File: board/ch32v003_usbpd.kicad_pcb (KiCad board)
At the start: 2 copper layers, 32 x 35 mm, 21 parts, among them J1 USB_C_Receptacle_USB2.0, J2 Conn_01x04_Pin, J3 VOUT, U1 CH32V003F4P6, U2 HT75xx-1-SOT89

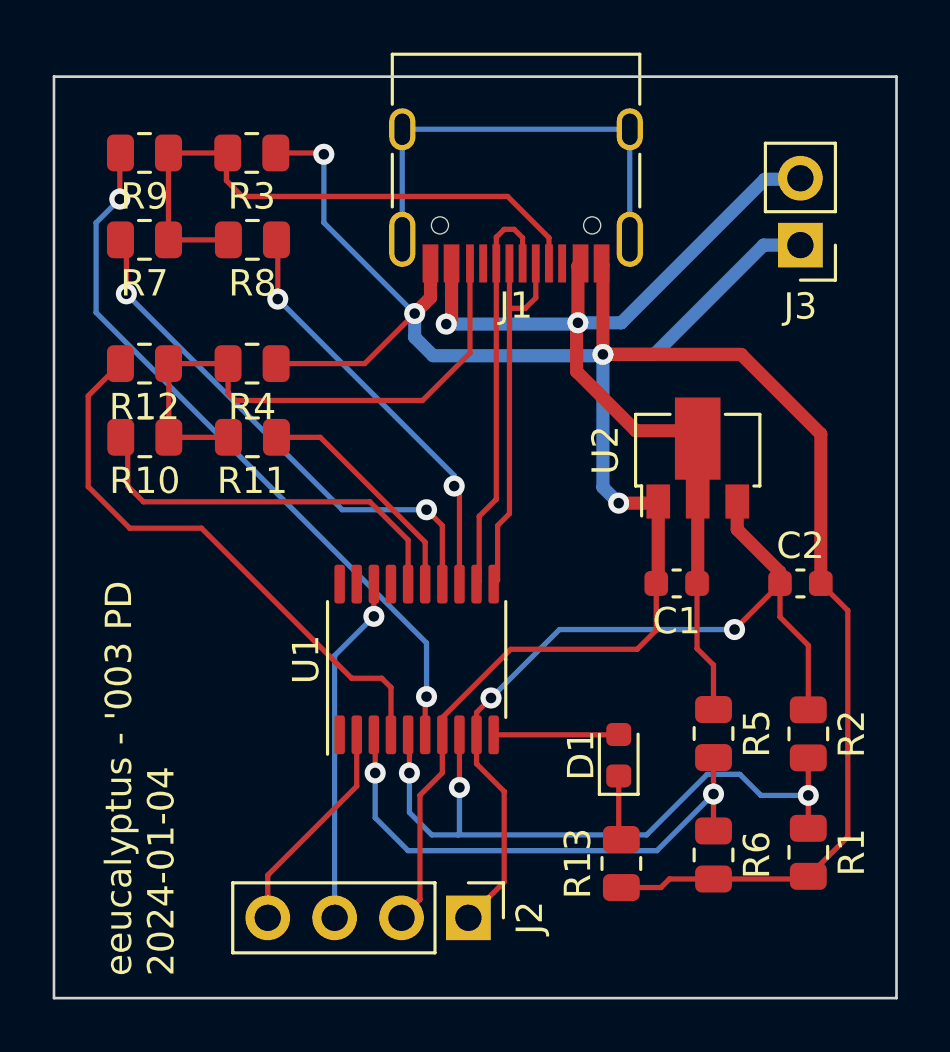
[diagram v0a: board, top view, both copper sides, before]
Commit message: Add test points to board
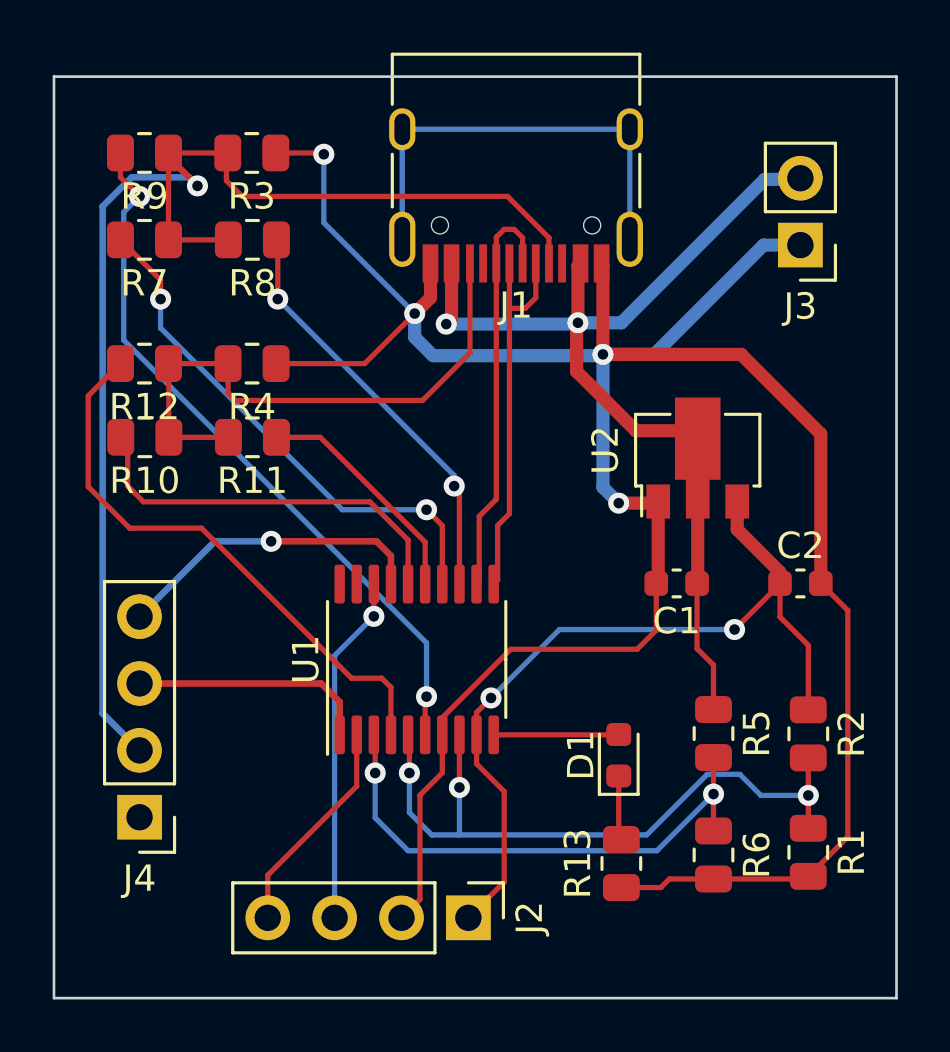
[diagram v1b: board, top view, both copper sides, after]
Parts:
- added J4: Test, Connector_PinHeader_2.54mm:PinHeader_1x04_P2.54mm_Vertical, F.Cu at (104.0, 50.5)
- R1: value R -> 470
- R2: value R -> 1K2
- R3: value R -> 5K1
- R7: value R -> 120
- R8: value R -> 75
- R9: value R -> 47
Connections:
- U1 pad 17: unconnected-(U1-PC7-Pad17) -> /Trigger
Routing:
- net /CC1: track 23.0 -> 50.2 mm, vias 0 -> 1
- net /Trigger: track 0.00 -> 12.0 mm, vias 0 -> 1
- net /OPO: track 0.00 -> 9.14 mm
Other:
- board text added: "eeucalyptus - '003 PD Rev. 2 2024-03-03"
- board text removed: "eeucalyptus - '003 PD 2024-01-04"
